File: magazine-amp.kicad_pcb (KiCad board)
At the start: 2 copper layers, 55 parts, among them J1 Input, J2 Output, J3 VCC, Q1 МП39Б, Q2 МП39Б, Q3 МП41, Q4 МП42Б, Q5 МП42Б, Q6 П214А, Q7 П214А

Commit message: Fix power nets
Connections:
- Q4 pad 3: /-20V -> -20V
- Q6 pad 3: /-20V -> -20V
- R10 pad 1: /-20V -> -20V
- R13 pad 1: /-20V -> -20V
- R20 pad 1: /-20V -> -20V
- RV4 pad 1: /-20V -> -20V
- RV4 pad 2: /-20V -> -20V
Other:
- net class Default: clearance 0.2 -> 0.3; trace_width 0.25 -> 0.35
- net class Power added: clearance 0.3, trace_width 0.8, via_dia 0.8, via_drill 0.4
- rule trace_clearance: 0.2 -> 0.3

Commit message: Assign footprints to components
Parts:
- added C1: 5u x 15V, Capacitor_THT:CP_Radial_D4.0mm_P2.00mm, F.Cu at (74.9, 80.4)
- added C2: 15u x 6V, Capacitor_THT:CP_Radial_D5.0mm_P2.00mm, F.Cu at (88.2, 89.8)
- added C3: 120p, Capacitor_THT:C_Rect_L4.6mm_W3.8mm_P2.50mm_MKS02_FKP02, F.Cu at (92.2, 82.7)
- added C4: 5u x 10V, Capacitor_THT:CP_Radial_D4.0mm_P2.00mm, F.Cu at (81.0, 95.9)
- added C5: 15u x 6V, Capacitor_THT:CP_Radial_D5.0mm_P2.00mm, F.Cu at (81.5, 89.8)
- added C6: 33u x 20V, Capacitor_THT:CP_Radial_D5.0mm_P2.00mm, F.Cu at (86.1, 83.3)
- added D1: Д813, Diode_THT:D_DO-201_P15.24mm_Horizontal, F.Cu at (43.5, 71.5)
- added J2: Output, Connector_PinSocket_2.54mm:PinSocket_1x02_P2.54mm_Vertical, F.Cu at (91.3, 75.2)
- added Q1: П28, Package_TO_SOT_THT:TO-11-3, F.Cu at (60.2, 89.8)
- added Q2: П28, Package_TO_SOT_THT:TO-11-3, F.Cu at (71.1, 89.8)
- added R1: 6.8K, Resistor_THT:R_Axial_DIN0309_L9.0mm_D3.2mm_P12.70mm_Horizontal, F.Cu at (62.4, 70.5)
- added R10: 1K, Resistor_THT:R_Axial_DIN0309_L9.0mm_D3.2mm_P12.70mm_Horizontal, F.Cu at (43.0, 77.2)
- added R2: 150, Resistor_THT:R_Axial_DIN0309_L9.0mm_D3.2mm_P12.70mm_Horizontal, F.Cu at (43.0, 82.0)
- added R3: 3K, Resistor_THT:R_Axial_DIN0309_L9.0mm_D3.2mm_P12.70mm_Horizontal, F.Cu at (58.8, 77.2)
- added R4: 75K, Resistor_THT:R_Axial_DIN0309_L9.0mm_D3.2mm_P12.70mm_Horizontal, F.Cu at (43.0, 86.7)
- added R5: 120K, Resistor_THT:R_Axial_DIN0309_L9.0mm_D3.2mm_P12.70mm_Horizontal, F.Cu at (43.0, 91.5)
- added R6: 8.2K, Resistor_THT:R_Axial_DIN0309_L9.0mm_D3.2mm_P12.70mm_Horizontal, F.Cu at (78.2, 70.5)
- added R7: 1.2K, Resistor_THT:R_Axial_DIN0309_L9.0mm_D3.2mm_P12.70mm_Horizontal, F.Cu at (43.0, 96.2)
- added R8: 1K, Resistor_THT:R_Axial_DIN0309_L9.0mm_D3.2mm_P12.70mm_Horizontal, F.Cu at (58.8, 82.0)
- added R9: 590, Resistor_THT:R_Axial_DIN0309_L9.0mm_D3.2mm_P12.70mm_Horizontal, F.Cu at (74.7, 75.2)
- C10: renamed from C4; footprint Capacitor_THT:CP_Radial_D10.0mm_P5.00mm -> Capacitor_THT:CP_Radial_D5.0mm_P2.00mm
- C11: renamed from C5; value 22n -> 0.022u
- C12: renamed from C6; value 100n -> 0.22u; footprint Capacitor_THT:C_Rect_L11.0mm_W3.4mm_P10.00mm_MKT -> Capacitor_THT:C_Disc_D14.5mm_W5.0mm_P7.50mm
- C13: renamed from C7; value 10n -> 0.1u; footprint Capacitor_THT:C_Disc_D4.7mm_W2.5mm_P5.00mm -> Capacitor_THT:C_Disc_D14.5mm_W5.0mm_P7.50mm
- C14: renamed from C8; value 100n -> 0.01u; footprint Capacitor_THT:C_Rect_L11.0mm_W3.4mm_P10.00mm_MKT -> Capacitor_THT:C_Disc_D7.5mm_W4.4mm_P5.00mm
- C15: renamed from C9; footprint Capacitor_THT:CP_Radial_D7.5mm_P2.50mm -> Capacitor_THT:CP_Radial_D4.0mm_P2.00mm
- C16: renamed from C10; footprint Capacitor_THT:CP_Radial_D12.5mm_P5.00mm -> Capacitor_THT:CP_Radial_D8.0mm_P3.50mm
- C17: renamed from C11; footprint Capacitor_THT:CP_Radial_D8.0mm_P3.50mm -> Capacitor_THT:CP_Radial_D5.0mm_P2.00mm
- C18: renamed from C12; value 1n -> 0.001u; footprint Capacitor_THT:C_Disc_D4.7mm_W2.5mm_P5.00mm -> Capacitor_THT:C_Rect_L4.6mm_W3.8mm_P2.50mm_MKS02_FKP02
- C19: renamed from C13; footprint Capacitor_THT:CP_Radial_D8.0mm_P3.50mm -> Capacitor_THT:CP_Radial_D5.0mm_P2.00mm
- C20: renamed from C14; footprint Capacitor_THT:CP_Radial_D8.0mm_P3.50mm -> Capacitor_THT:CP_Radial_D5.0mm_P2.00mm
- C9: renamed from C3; footprint Capacitor_THT:CP_Radial_D7.5mm_P2.50mm -> Capacitor_THT:CP_Radial_D4.0mm_P2.00mm
- J3: value VCC -> Input
- R11: renamed from R1; footprint Resistor_THT:R_Axial_DIN0414_L11.9mm_D4.5mm_P15.24mm_Horizontal -> Resistor_THT:R_Axial_DIN0309_L9.0mm_D3.2mm_P12.70mm_Horizontal
- R12: renamed from R2; footprint Resistor_THT:R_Axial_DIN0414_L11.9mm_D4.5mm_P15.24mm_Horizontal -> Resistor_THT:R_Axial_DIN0309_L9.0mm_D3.2mm_P12.70mm_Horizontal
- R13: renamed from R3; footprint Resistor_THT:R_Axial_DIN0414_L11.9mm_D4.5mm_P15.24mm_Horizontal -> Resistor_THT:R_Axial_DIN0309_L9.0mm_D3.2mm_P12.70mm_Horizontal
- R14: renamed from R4; footprint Resistor_THT:R_Axial_DIN0414_L11.9mm_D4.5mm_P15.24mm_Horizontal -> Resistor_THT:R_Axial_DIN0309_L9.0mm_D3.2mm_P12.70mm_Horizontal
- R15: renamed from R5; footprint Resistor_THT:R_Axial_DIN0414_L11.9mm_D4.5mm_P15.24mm_Horizontal -> Resistor_THT:R_Axial_DIN0309_L9.0mm_D3.2mm_P12.70mm_Horizontal
- R16: renamed from R6; footprint Resistor_THT:R_Axial_DIN0414_L11.9mm_D4.5mm_P15.24mm_Horizontal -> Resistor_THT:R_Axial_DIN0309_L9.0mm_D3.2mm_P12.70mm_Horizontal
- R17: renamed from R7; value 6K2 -> 6.2K; footprint Resistor_THT:R_Axial_DIN0414_L11.9mm_D4.5mm_P15.24mm_Horizontal -> Resistor_THT:R_Axial_DIN0309_L9.0mm_D3.2mm_P12.70mm_Horizontal
- R18: renamed from R8; footprint Resistor_THT:R_Axial_DIN0414_L11.9mm_D4.5mm_P15.24mm_Horizontal -> Resistor_THT:R_Axial_DIN0309_L9.0mm_D3.2mm_P12.70mm_Horizontal
- R19: renamed from R9; footprint Resistor_THT:R_Axial_DIN0414_L11.9mm_D4.5mm_P15.24mm_Horizontal -> Resistor_THT:R_Axial_DIN0309_L9.0mm_D3.2mm_P12.70mm_Horizontal
- R20: renamed from R10; footprint Resistor_THT:R_Axial_DIN0414_L11.9mm_D4.5mm_P15.24mm_Horizontal -> Resistor_THT:R_Axial_DIN0309_L9.0mm_D3.2mm_P12.70mm_Horizontal
- R21: renamed from R11; footprint Resistor_THT:R_Axial_DIN0414_L11.9mm_D4.5mm_P15.24mm_Horizontal -> Resistor_THT:R_Axial_DIN0309_L9.0mm_D3.2mm_P12.70mm_Horizontal
- R22: renamed from R12; footprint Resistor_THT:R_Axial_DIN0414_L11.9mm_D4.5mm_P15.24mm_Horizontal -> Resistor_THT:R_Axial_DIN0309_L9.0mm_D3.2mm_P12.70mm_Horizontal
- R23: renamed from R13; footprint Resistor_THT:R_Axial_DIN0414_L11.9mm_D4.5mm_P15.24mm_Horizontal -> Resistor_THT:R_Axial_DIN0309_L9.0mm_D3.2mm_P12.70mm_Horizontal
- R24: renamed from R14; footprint Resistor_THT:R_Axial_DIN0414_L11.9mm_D4.5mm_P15.24mm_Horizontal -> Resistor_THT:R_Axial_DIN0309_L9.0mm_D3.2mm_P12.70mm_Horizontal
- R25: renamed from R15; footprint Resistor_THT:R_Axial_DIN0414_L11.9mm_D4.5mm_P15.24mm_Horizontal -> Resistor_THT:R_Axial_DIN0309_L9.0mm_D3.2mm_P12.70mm_Horizontal
- R26: renamed from R16; footprint Resistor_THT:R_Axial_DIN0414_L11.9mm_D4.5mm_P15.24mm_Horizontal -> Resistor_THT:R_Axial_DIN0309_L9.0mm_D3.2mm_P12.70mm_Horizontal
- R27: renamed from R17; footprint Resistor_THT:R_Axial_DIN0414_L11.9mm_D4.5mm_P15.24mm_Horizontal -> Resistor_THT:R_Axial_DIN0309_L9.0mm_D3.2mm_P12.70mm_Horizontal
- R28: renamed from R18; footprint Resistor_THT:R_Axial_DIN0414_L11.9mm_D4.5mm_P15.24mm_Horizontal -> Resistor_THT:R_Axial_DIN0309_L9.0mm_D3.2mm_P12.70mm_Horizontal
- R29: renamed from R19; footprint Resistor_THT:R_Axial_DIN0414_L11.9mm_D4.5mm_P15.24mm_Horizontal -> Resistor_THT:R_Axial_DIN0309_L9.0mm_D3.2mm_P12.70mm_Horizontal
- R30: renamed from R20; value 2K4 -> 2.4K; footprint Resistor_THT:R_Axial_DIN0414_L11.9mm_D4.5mm_P15.24mm_Horizontal -> Resistor_THT:R_Axial_DIN0309_L9.0mm_D3.2mm_P12.70mm_Horizontal
- R31: renamed from R21; footprint Resistor_THT:R_Axial_DIN0414_L11.9mm_D4.5mm_P15.24mm_Horizontal -> Resistor_THT:R_Axial_DIN0309_L9.0mm_D3.2mm_P12.70mm_Horizontal
- R32: renamed from R22; value 1K8 -> 1.8K; footprint Resistor_THT:R_Axial_DIN0414_L11.9mm_D4.5mm_P15.24mm_Horizontal -> Resistor_THT:R_Axial_DIN0309_L9.0mm_D3.2mm_P12.70mm_Horizontal
- R33: renamed from R23; footprint Resistor_THT:R_Axial_DIN0414_L11.9mm_D4.5mm_P15.24mm_Horizontal -> Resistor_THT:R_Axial_DIN0309_L9.0mm_D3.2mm_P12.70mm_Horizontal
- R34: renamed from R24; footprint Resistor_THT:R_Axial_DIN0414_L11.9mm_D4.5mm_P15.24mm_Horizontal -> Resistor_THT:R_Axial_DIN0309_L9.0mm_D3.2mm_P12.70mm_Horizontal
- R35: renamed from R25; footprint Resistor_THT:R_Axial_DIN0614_L14.3mm_D5.7mm_P15.24mm_Horizontal -> Resistor_THT:R_Axial_DIN0918_L18.0mm_D9.0mm_P25.40mm_Horizontal
- R36: renamed from R26; footprint Resistor_THT:R_Axial_DIN0614_L14.3mm_D5.7mm_P15.24mm_Horizontal -> Resistor_THT:R_Axial_DIN0918_L18.0mm_D9.0mm_P25.40mm_Horizontal
- RV5: value 2K2 -> 2.2K
- moved C7 228.3 mm to (261.2, -46.1)
- moved C8 228.3 mm to (269.2, -46.1)
- moved C9 228.3 mm to (246.2, -14.1)
- moved J3 228.3 mm to (285.2, -61.1)
- moved J4 228.3 mm to (270.2, -61.1)
- moved Q3 228.3 mm to (246.2, -29.1)
- moved R11 228.3 mm to (271.2, -52.1)
- moved R12 228.3 mm to (256.2, -40.1)
- moved R13 228.3 mm to (256.2, -33.1)
- moved R14 228.3 mm to (235.2, -40.1)
- moved R15 228.3 mm to (292.2, -20.1)
- moved R18 228.3 mm to (277.2, -26.1)
- moved R19 228.3 mm to (277.2, -33.1)
- moved R20 228.3 mm to (292.2, -40.1)
- moved RV1 228.3 mm to (246.2, -6.14)
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- renumbered C1 to C7, C2 to C8, J2 to J4, Q1 to Q3, Q2 to Q4, Q3 to Q5, Q4 to Q6, Q5 to Q7, Q6 to Q8, Q7 to Q9
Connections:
- C7 pad 2: Net-(C1-Pad2) -> Net-(C7-Pad2)
- J1 pad 1: Net-(C1-Pad2) -> Net-(C1-Pad1)
- J3 pad 1: /-20V -> Net-(C7-Pad2)
- R11 pad 2: Net-(C1-Pad2) -> Net-(C7-Pad2)

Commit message: Route preamp
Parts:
- added J5: Power, Connector_PinSocket_2.54mm:PinSocket_1x02_P2.54mm_Vertical, F.Cu at (67.9, 54.0)
- moved J3 242.9 mm to (83.2, 73.7), turned to 0 degrees
- moved R11 210.1 mm to (102.9, 73.7)
- moved C8 208.8 mm to (102.9, 80.0), turned to 90 degrees
- moved C7 208.1 mm to (95.2, 79.4)
- moved R14 191.2 mm to (90.2, 84.5)
- moved R12 188.0 mm to (102.9, 68.6), turned to 180 degrees
- moved R13 181.2 mm to (102.9, 63.5), turned to 180 degrees
- moved Q3 172.8 mm to (109.2, 76.2), turned to 0 degrees
- moved C9 155.2 mm to (121.9, 78.7)
- moved RV1 141.7 mm to (134.6, 81.3)
- moved C6 54.6 mm to (34.3, 66.0)
- moved C1 43.7 mm to (31.8, 73.7)
- moved C3 37.4 mm to (55.2, 76.8), turned to 180 degrees
- moved R1 34.6 mm to (30.5, 83.8)
- moved R6 33.0 mm to (47.0, 59.7)
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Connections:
- C4 pad 2: Net-(C4-Pad2) -> Net-(C3-Pad1)
- Q2 pad 3: Net-(C4-Pad2) -> Net-(C3-Pad1)
- R6 pad 2: Net-(C4-Pad2) -> Net-(C3-Pad1)
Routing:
- net GND: track 0.00 -> 79.1 mm
- net Net-(C3-Pad1): track 0.00 -> 48.7 mm
- net Net-(C5-Pad2): track 0.00 -> 35.2 mm
- net Net-(C6-Pad2): track 0.00 -> 25.4 mm
- net Net-(Q1-Pad3): track 0.00 -> 24.3 mm
- net Net-(C3-Pad2): track 0.00 -> 22.3 mm
- net Net-(R1-Pad2): track 0.00 -> 20.8 mm
- net Net-(C1-Pad2): track 0.00 -> 19.7 mm
- net Net-(C2-Pad2): track 0.00 -> 11.5 mm
- net Net-(C1-Pad1): track 0.00 -> 10.2 mm
- net -20V: track 0.00 -> 8.52 mm
- net Net-(C4-Pad1): track 0.00 -> 6.61 mm
- net Net-(C5-Pad1): track 0.00 -> 6.50 mm

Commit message: Route power amplifier
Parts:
- moved C10 268.8 mm to (83.8, 63.5)
- moved R16 242.8 mm to (90.2, 90.2)
- moved RV4 230.7 mm to (109.2, 53.3), turned to 90 degrees
- moved C15 217.7 mm to (152.4, 67.3)
- moved R19 208.2 mm to (90.2, 58.4)
- moved R20 207.9 mm to (102.9, 53.3)
- moved Q5 202.5 mm to (161.3, 66.0)
- moved R21 190.8 mm to (161.3, 86.4), turned to 90 degrees
- moved C18 187.6 mm to (182.9, 81.3), turned to 180 degrees
- moved Q4 184.9 mm to (143.5, 68.6), turned to 90 degrees
- moved C14 184.1 mm to (115.6, 62.2), turned to 270 degrees
- moved C19 179.2 mm to (175.3, 92.7), turned to 90 degrees
- moved C12 179.2 mm to (133.3, 83.8), turned to 90 degrees
- moved R15 178.8 mm to (148.6, 86.4), turned to 90 degrees
- moved C13 175.9 mm to (141.0, 83.8), turned to 90 degrees
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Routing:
- net Net-(C16-Pad1): track 0.00 -> 126.5 mm
- net -20V: track 8.52 -> 90.8 mm
- net Net-(C19-Pad1): track 0.00 -> 66.4 mm
- net Net-(C15-Pad1): track 0.00 -> 60.6 mm
- net Net-(C17-Pad1): track 0.00 -> 58.8 mm
- net GND: track 79.1 -> 117.6 mm
- net Net-(C11-Pad2): track 0.00 -> 37.9 mm
- net Net-(C12-Pad2): track 0.00 -> 37.4 mm
- net Net-(C13-Pad1): track 0.00 -> 36.3 mm
- net Net-(C18-Pad2): track 0.00 -> 34.8 mm
- net Net-(Q7-Pad2): track 0.00 -> 31.3 mm
- net Net-(Q6-Pad2): track 0.00 -> 30.0 mm
- net Net-(C7-Pad1): track 0.00 -> 28.3 mm
- net Net-(C11-Pad1): track 0.00 -> 21.9 mm
- net Net-(C15-Pad2): track 0.00 -> 21.4 mm
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
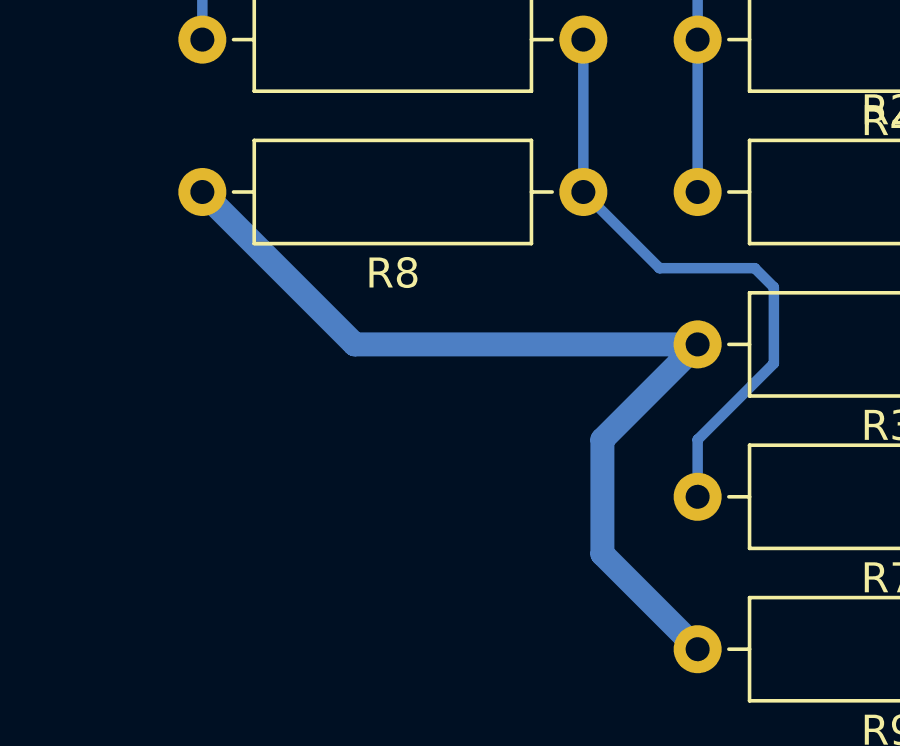
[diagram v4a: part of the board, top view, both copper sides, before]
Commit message: Fix ground traces
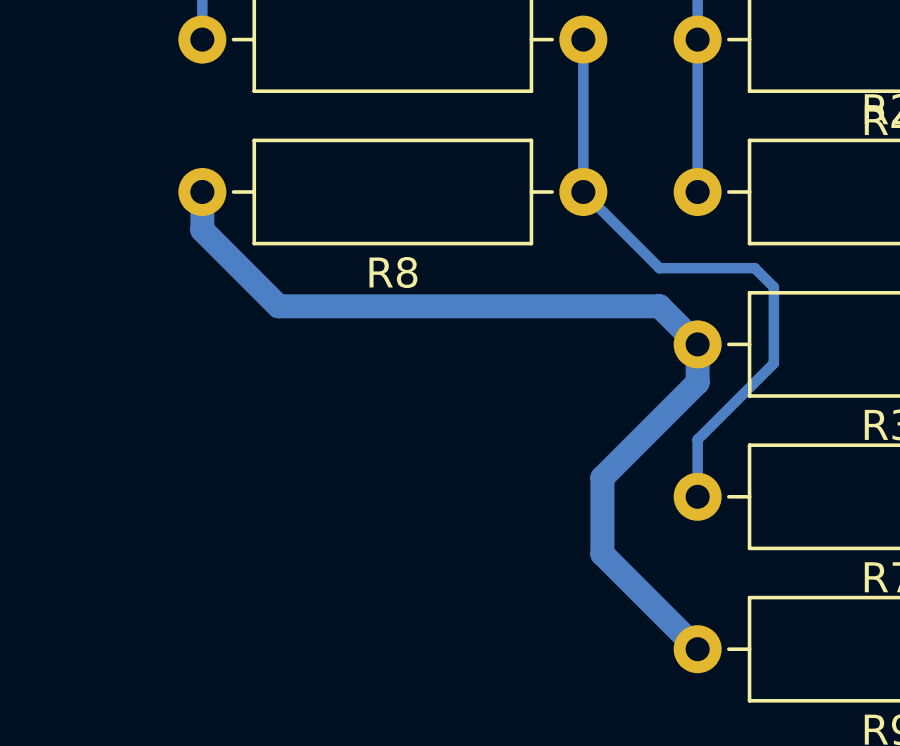
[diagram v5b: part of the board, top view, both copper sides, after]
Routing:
- net GND: track 117.6 -> 118.3 mm
